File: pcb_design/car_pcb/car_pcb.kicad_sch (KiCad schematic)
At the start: 28 parts, among them J1 PICO_R, J10 CMD_UART, J11 +5V, J12 PICO_L, J14 PWR_OUTPUT, J16 NRF24L01, J18 GND, J19 +3.3V, J2 PWR_INPUT, J20 GND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

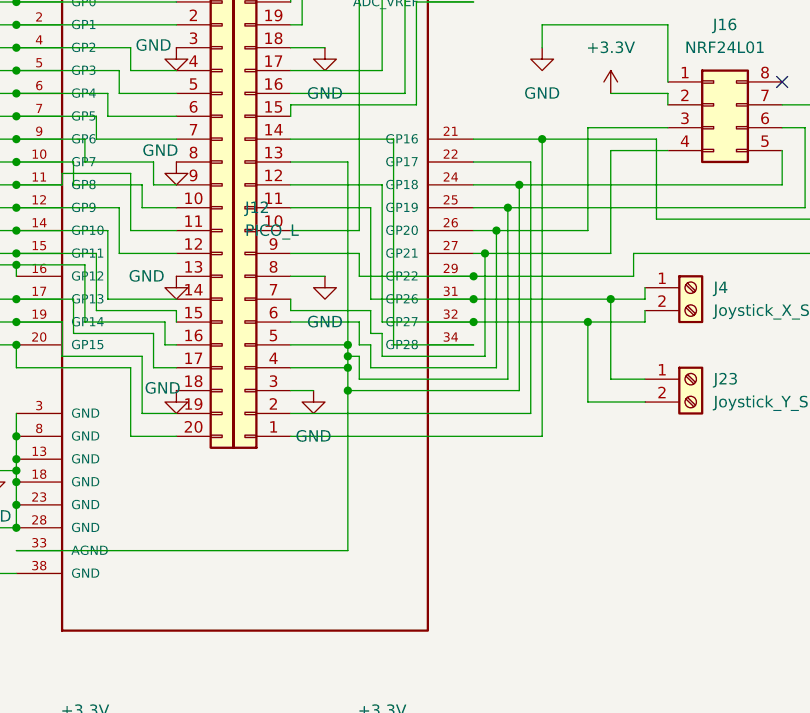
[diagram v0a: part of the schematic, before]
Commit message: fix issue with mistakes in rev 1.1. Now rev 1.2 is ready
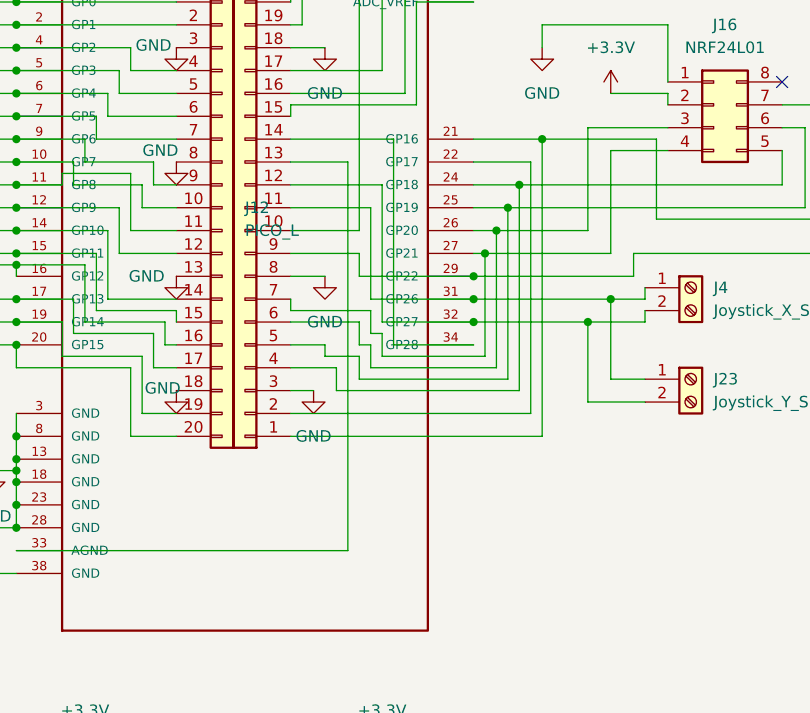
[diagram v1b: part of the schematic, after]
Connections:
- new net: A1.24 (GP18), J1.4 (Pin_4), J16.5 (Pin_5)
- new net: A1.25 (GP19), J1.5 (Pin_5), J16.6 (Pin_6)
- new net: A1.33 (AGND), J1.13 (Pin_13)
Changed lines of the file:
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@@
-	)
-	(junction
-		(at 215.9 85.09)
-		(diameter 0)
-		(color 0 0 0 0)
 	)
 	(junction
@@
 	)
 	(junction
-		(at 215.9 86.36)
-		(diameter 0)
-		(color 0 0 0 0)
-	)
-	(junction
 		(at 179.07 64.77)
 		(diameter 0)
@@
 	)
 	(junction
-		(at 215.9 87.63)
-		(diameter 0)
-		(color 0 0 0 0)
-	)
-	(junction
 		(at 17.78 127)
 		(diameter 0)
@@
 	(junction
 		(at 179.07 57.15)
-		(diameter 0)
-		(color 0 0 0 0)
-	)
-	(junction
-		(at 215.9 90.17)
 		(diameter 0)
 		(color 0 0 0 0)
@@
 	(wire
 		(pts
-			(xy 215.9 90.17) (xy 215.9 107.95)
-		)
-		(stroke
-			(width 0)
-			(type default)
-		)
-	)
-	(wire
-		(pts
 			(xy 173.99 45.72) (xy 168.91 45.72)
 		)
@@
 	(wire
 		(pts
-			(xy 215.9 64.77) (xy 215.9 85.09)
-		)
-		(stroke
-			(width 0)
-			(type default)
-		)
-	)
-	(wire
-		(pts
 			(xy 186.69 82.55) (xy 195.58 82.55)
 		)
@@
 	(wire
 		(pts
-			(xy 215.9 90.17) (xy 234.95 90.17)
-		)
-		(stroke
-			(width 0)
-			(type default)
-		)
-	)
-	(wire
-		(pts
 			(xy 251.46 57.15) (xy 251.46 58.42)
 		)
@@
 	(wire
 		(pts
+			(xy 213.36 86.36) (xy 217.17 86.36)
+		)
+		(stroke
+			(width 0)
+			(type default)
+		)
+	)
+	(wire
+		(pts
 			(xy 237.49 62.23) (xy 250.19 62.23)
 		)
@@
 	(wire
 		(pts
+			(xy 209.55 85.09) (xy 213.36 85.09)
+		)
+		(stroke
+			(width 0)
+			(type default)
+		)
+	)
+	(wire
+		(pts
+			(xy 217.17 86.36) (xy 217.17 88.9)
+		)
+		(stroke
+			(width 0)
+			(type default)
+		)
+	)
+	(wire
+		(pts
 			(xy 189.23 59.69) (xy 196.85 59.69)
 		)
@@
 	(wire
 		(pts
+			(xy 213.36 85.09) (xy 213.36 86.36)
+		)
+		(stroke
+			(width 0)
+			(type default)
+		)
+	)
+	(wire
+		(pts
 			(xy 232.41 72.39) (xy 232.41 87.63)
 		)
@@
 	(wire
 		(pts
-			(xy 215.9 85.09) (xy 209.55 85.09)
-		)
-		(stroke
-			(width 0)
-			(type default)
-		)
-	)
-	(wire
-		(pts
 			(xy 187.96 62.23) (xy 196.85 62.23)
 		)
@@
 	(wire
 		(pts
-			(xy 217.17 86.36) (xy 215.9 86.36)
-		)
-		(stroke
-			(width 0)
-			(type default)
-		)
-	)
-	(wire
-		(pts
 			(xy 233.68 69.85) (xy 266.7 69.85)
 		)
@@
 	(wire
 		(pts
+			(xy 214.63 87.63) (xy 214.63 90.17)
+		)
+		(stroke
+			(width 0)
+			(type default)
+		)
+	)
+	(wire
+		(pts
 			(xy 229.87 69.85) (xy 233.68 69.85)
 		)
@@
 	(wire
 		(pts
-			(xy 217.17 88.9) (xy 217.17 86.36)
-		)
-		(stroke
-			(width 0)
-			(type default)
-		)
-	)
-	(wire
-		(pts
 			(xy 242.57 72.39) (xy 242.57 60.96)
 		)
@@
 	(wire
 		(pts
-			(xy 209.55 87.63) (xy 215.9 87.63)
-		)
-		(stroke
-			(width 0)
-			(type default)
-		)
-	)
-	(wire
-		(pts
 			(xy 165.1 59.69) (xy 179.07 59.69)
 		)
@@
 	(wire
 		(pts
-			(xy 215.9 87.63) (xy 215.9 90.17)
+			(xy 215.9 64.77) (xy 215.9 107.95)
 		)
 		(stroke
@@
 	(wire
 		(pts
-			(xy 215.9 86.36) (xy 215.9 87.63)
-		)
-		(stroke
-			(width 0)
-			(type default)
-		)
-	)
-	(wire
-		(pts
 			(xy 168.91 44.45) (xy 168.91 45.72)
 		)
@@
 	(wire
 		(pts
-			(xy 215.9 85.09) (xy 215.9 86.36)
-		)
-		(stroke
-			(width 0)
-			(type default)
-		)
-	)
-	(wire
-		(pts
 			(xy 179.07 80.01) (xy 185.42 80.01)
 		)
@@
 	(wire
 		(pts
+			(xy 209.55 87.63) (xy 214.63 87.63)
+		)
+		(stroke
+			(width 0)
+			(type default)
+		)
+	)
+	(wire
+		(pts
 			(xy 179.07 72.39) (xy 189.23 72.39)
 		)
@@
 		)
 		(stroke
+			(width 0)
+			(type default)
+		)
+	)
+	(wire
+		(pts
+			(xy 214.63 90.17) (xy 234.95 90.17)
+		)
+		(stroke
